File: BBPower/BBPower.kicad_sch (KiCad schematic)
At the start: 22 parts, among them J1 USB_C_Receptacle, J2 Conn_01x04, J3 Conn_01x04, J4 Conn_01x04, J5 Conn_01x04, J6 Screw_Terminal_01x02, SW1 SW_DIP_x03, SW2 OS103012MU2QP1, SW3 OS103012MU2QP1, U1 CH224K, U2 LM317_SOT-223, U3 LM317_SOT-223

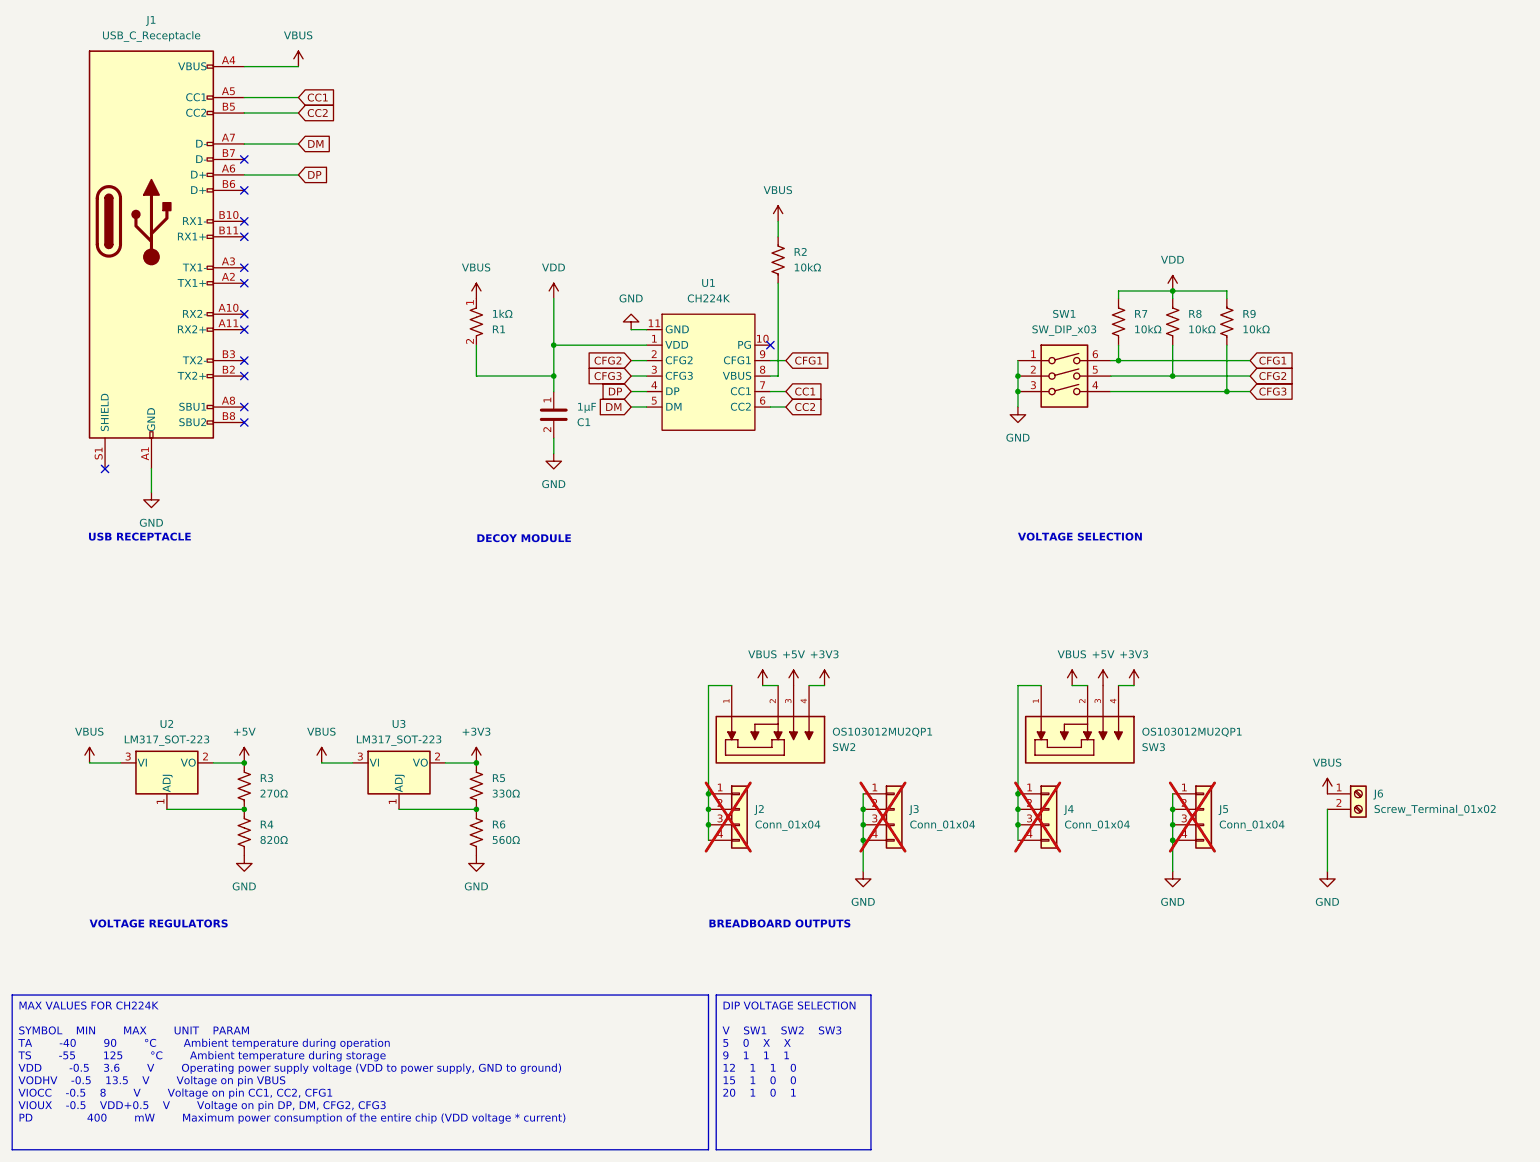
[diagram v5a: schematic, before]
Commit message: fixed bom & updated prod files
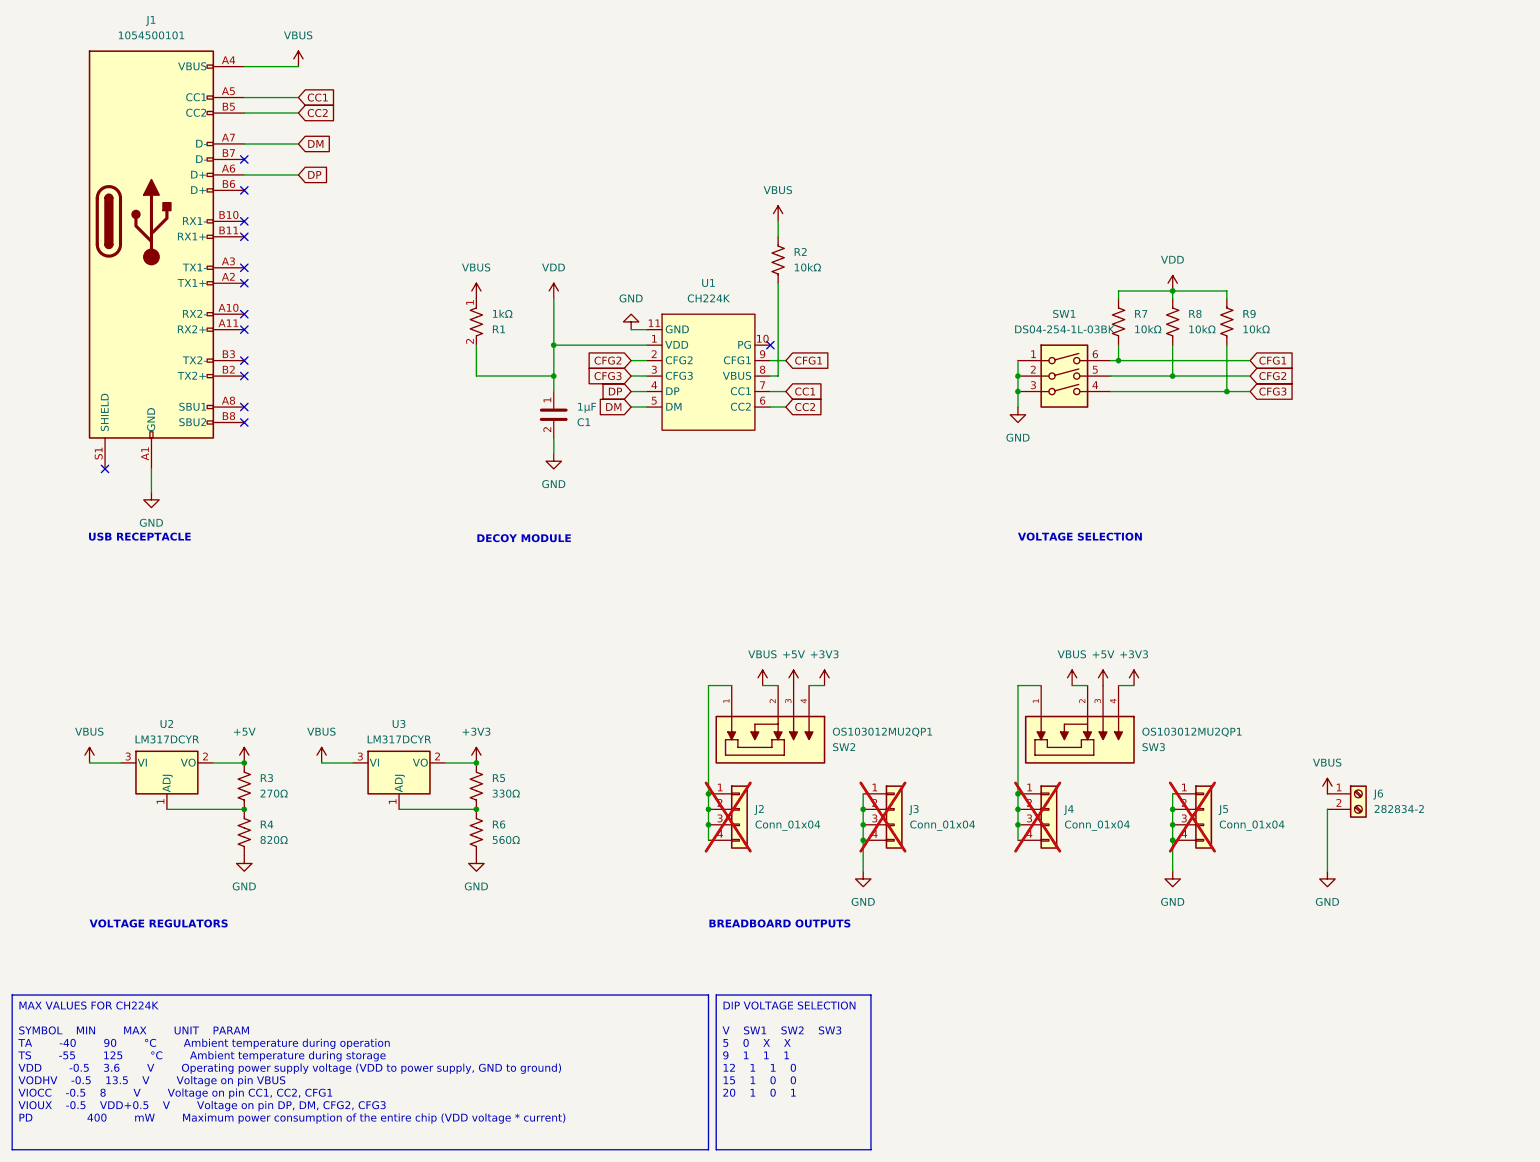
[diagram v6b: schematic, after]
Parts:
- C1: MANUFACTURER (none) -> Samsung Electro-Mechanics
- J1: value USB_C_Receptacle -> 1054500101; MANUFACTURER (none) -> Molex
- J6: value Screw_Terminal_01x02 -> 282834-2; MANUFACTURER (none) -> TE Connectivity AMP Connectors
- R1, R2, R3, R4, R5, R6, R7, R8, R9: MANUFACTURER (none) -> Vishay Dale
- SW1: value SW_DIP_x03 -> DS04-254-1L-03BK; MANUFACTURER (none) -> Same Sky (Formerly CUI Devices)
- SW2, SW3: MANUFACTURER CnK -> C&K
- U2, U3: value LM317_SOT-223 -> LM317DCYR; MANUFACTURER (none) -> Texas Instruments
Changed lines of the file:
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@@
 			)
 		)
-		(property "Description" "Resistor, US symbol"
+		(property "Description" "RES SMD 10K OHM 1% 3/4W 1206"
+			(at 203.2 67.31 0)
+			(effects
+				(font
+					(size 1.27 1.27)
+				)
+				(hide yes)
+			)
+		)
+		(property "MANUFACTURER" "Vishay Dale"
 			(at 203.2 67.31 0)
 			(effects
@@
 			)
 		)
-		(property "Description" "Resistor, US symbol"
+		(property "Description" "RES SMD 820 OHM 1% 3/4W 1206"
+			(at 50.8 151.13 0)
+			(effects
+				(font
+					(size 1.27 1.27)
+				)
+				(hide yes)
+			)
+		)
+		(property "MANUFACTURER" "Vishay Dale"
 			(at 50.8 151.13 0)
 			(effects
@@
 			)
 		)
-		(property "Description" "Resistor, US symbol"
+		(property "Description" "RES SMD 560 OHM 1% 3/4W 1206"
+			(at 88.9 151.13 0)
+			(effects
+				(font
+					(size 1.27 1.27)
+				)
+				(hide yes)
+			)
+		)
+		(property "MANUFACTURER" "Vishay Dale"
 			(at 88.9 151.13 0)
 			(effects
@@
 			)
 		)
-		(property "Description" "Unpolarized capacitor"
+		(property "Description" "CAP CER 1UF 25V X7R 1206"
+			(at 101.6 82.55 0)
+			(effects
+				(font
+					(size 1.27 1.27)
+				)
+				(hide yes)
+			)
+		)
+		(property "MANUFACTURER" "Samsung Electro-Mechanics"
 			(at 101.6 82.55 0)
 			(effects
@@
 			)
 		)
-		(property "Description" "Resistor, US symbol"
+		(property "Description" "RES SMD 330 OHM 1% 3/4W 1206"
+			(at 88.9 143.51 0)
+			(effects
+				(font
+					(size 1.27 1.27)
+				)
+				(hide yes)
+			)
+		)
+		(property "MANUFACTURER" "Vishay Dale"
 			(at 88.9 143.51 0)
 			(effects
@@
 			)
 		)
-		(property "Description" ""
+		(property "Description" "WITCH SLIDE SP3T 200MA 30V"
 			(at 186.69 134.62 0)
 			(effects
@@
 			)
 		)
-		(property "MANUFACTURER" "CnK"
+		(property "MANUFACTURER" "C&K"
 			(at 186.69 134.62 0)
 			(effects
@@
 			)
 		)
-		(property "Value" "LM317_SOT-223"
+		(property "Value" "LM317DCYR"
 			(at 76.2 135.89 0)
 			(effects
@@
 			)
 		)
-		(property "Description" "1.5A 35V Adjustable Linear Regulator, SOT-223"
+		(property "Description" "IC REG LIN POS ADJ 1.5A SOT223-4"
+			(at 76.2 139.7 0)
+			(effects
+				(font
+					(size 1.27 1.27)
+				)
+				(hide yes)
+			)
+		)
+		(property "MANUFACTURER" "Texas Instruments"
 			(at 76.2 139.7 0)
 			(effects
@@
 			)
 		)
-		(property "Description" "Resistor, US symbol"
+		(property "Description" "RES SMD 10K OHM 1% 3/4W 1206"
+			(at 138.43 57.15 0)
+			(effects
+				(font
+					(size 1.27 1.27)
+				)
+				(hide yes)
+			)
+		)
+		(property "MANUFACTURER" "Vishay Dale"
 			(at 138.43 57.15 0)
 			(effects
@@
 			)
 		)
-		(property "Description" "Resistor, US symbol"
+		(property "Description" "RES SMD 10K OHM 1% 3/4W 1206"
+			(at 194.31 67.31 0)
+			(effects
+				(font
+					(size 1.27 1.27)
+				)
+				(hide yes)
+			)
+		)
+		(property "MANUFACTURER" "Vishay Dale"
 			(at 194.31 67.31 0)
 			(effects
@@
 			)
 		)
-		(property "Description" "Resistor, US symbol"
+		(property "Description" "RES SMD 270 OHM 1% 3/4W 1206"
+			(at 50.8 143.51 0)
+			(effects
+				(font
+					(size 1.27 1.27)
+				)
+				(hide yes)
+			)
+		)
+		(property "MANUFACTURER" "Vishay Dale"
 			(at 50.8 143.51 0)
 			(effects
@@
 			)
 		)
-		(property "Description" "Resistor, US symbol"
+		(property "Description" "RES SMD 1K OHM 1% 3/4W 1206"
+			(at 88.9 67.31 0)
+			(effects
+				(font
+					(size 1.27 1.27)
+				)
+				(hide yes)
+			)
+		)
+		(property "MANUFACTURER" "Vishay Dale"
 			(at 88.9 67.31 0)
 			(effects
@@
 			)
 		)
-		(property "Value" "USB_C_Receptacle"
+		(property "Value" "1054500101"
 			(at 35.56 20.32 0)
 			(effects
@@
 			)
 		)
-		(property "Description" "USB Full-Featured Type-C Receptacle connector"
+		(property "Description" "CONN RCP USB3.1 TYPEC 24P SMD RA"
+			(at 35.56 50.8 0)
+			(effects
+				(font
+					(size 1.27 1.27)
+				)
+				(hide yes)
+			)
+		)
+		(property "MANUFACTURER" "Molex"
 			(at 35.56 50.8 0)
 			(effects
@@
 			)
 		)
-		(property "Value" "Screw_Terminal_01x02"
+		(property "Value" "282834-2"
 			(at 236.22 147.3199 0)
 			(effects
@@
 			)
 		)
-		(property "Description" "Generic screw terminal, single row, 01x02, script generated (kicad-library-utils/schlib/autogen/connector/)"
+		(property "Description" "TERM BLK 2P SIDE ENT 2.54MM PCB"
+			(at 233.68 144.78 0)
+			(effects
+				(font
+					(size 1.27 1.27)
+				)
+				(hide yes)
+			)
+		)
+		(property "MANUFACTURER" "TE Connectivity AMP Connectors"
 			(at 233.68 144.78 0)
 			(effects
@@
 			)
 		)
-		(property "Value" "SW_DIP_x03"
+		(property "Value" "DS04-254-1L-03BK"
 			(at 185.42 68.58 0)
 			(effects
@@
 			)
 		)
-		(property "Description" "3x DIP Switch, Single Pole Single Throw (SPST) switch, small symbol"
+		(property "Description" "SWITCH SLIDE DIP SPST 0.025A 24V"
+			(at 185.42 76.2 0)
+			(effects
+				(font
+					(size 1.27 1.27)
+				)
+				(hide yes)
+			)
+		)
+		(property "MANUFACTURER" "Same Sky (Formerly CUI Devices)"
 			(at 185.42 76.2 0)
 			(effects
@@
 			)
 		)
-		(property "Description" ""
+		(property "Description" "WITCH SLIDE SP3T 200MA 30V"
 			(at 135.89 134.62 0)
 			(effects
@@
 			)
 		)
-		(property "MANUFACTURER" "CnK"
+		(property "MANUFACTURER" "C&K"
 			(at 135.89 134.62 0)
 			(effects
@@
 			)
 		)
-		(property "Description" "Resistor, US symbol"
+		(property "Description" "RES SMD 10K OHM 1% 3/4W 1206"
+			(at 212.09 67.31 0)
+			(effects
+				(font
+					(size 1.27 1.27)
+				)
+				(hide yes)
+			)
+		)
+		(property "MANUFACTURER" "Vishay Dale"
 			(at 212.09 67.31 0)
 			(effects
@@
 			)
 		)
-		(property "Value" "LM317_SOT-223"
+		(property "Value" "LM317DCYR"
 			(at 38.1 135.89 0)
 			(effects
@@
 			)
 		)
-		(property "Description" "1.5A 35V Adjustable Linear Regulator, SOT-223"
+		(property "Description" "IC REG LIN POS ADJ 1.5A SOT223-4"
+			(at 38.1 139.7 0)
+			(effects
+				(font
+					(size 1.27 1.27)
+				)
+				(hide yes)
+			)
+		)
+		(property "MANUFACTURER" "Texas Instruments"
 			(at 38.1 139.7 0)
 			(effects
